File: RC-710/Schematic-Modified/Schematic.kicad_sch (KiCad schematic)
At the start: 66 parts, among them K1 Fujitsu_FTR-LYAA005x, Q1 NPN, Q2 NPN, SW1 ON/OFF, SW2 LEARN, U1 LM358, U2 4N25, Y1 Crystal

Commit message: Schematic: Improved layout
Signed-off-by: Patrick Pedersen <ctx.xda@gmail.com>
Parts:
- removed R25: R, symbol Device:R
- removed U2: 4N25, Package_DIP:DIP-6_W7.62mm, symbol Isolator:4N25
- added R13: R, symbol Device:R
- added R14: 5V: 380R / 3V3: 210R, symbol Device:R
- added U2: ~, symbol RC-710:Blob_IC
- added U3: 4N25, Package_DIP:DIP-6_W7.62mm, symbol Isolator:4N25
- Y1: value Crystal -> 455kHZ
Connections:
- net Blob IC PB LEARN: now also U2. (VCC)
- net Blob IC PB ON/OFF: now also U2. (VCC)
- net Blob IC REF CLK A: now also U2. (VCC)
- net Blob IC REF CLK B: now also U2. (VCC)
- net Blob IC SIGNAL: now also U2. (VCC)
- net GND: now also U2. (VCC), U3.4
- net Pi Pico W GND: now also U3.2
- net V1: no longer C11.1, C16.2, D10.2 (A), D13.1 (K), R16.1, R23.1, R7.1, U1.8 (V+)
- net Blob IC RST?: no longer names the net of TP2.1
- net Blob IC RST?: now also R13.1, U2. (VCC)
- net Blob IC UNKNOWN: no longer names the net of TP1.1
- net Blob IC UNKNOWN: now also U2. (VCC)
- net Blob IC VCC? renamed +3V0
- net +3V0: now also R13.2, U2. (VCC)
- net ~{Blob IC RELAY} renamed Blob IC RELAY
- net Blob IC RELAY: now also U2. (VCC), U3.6
- new net: R14.2, U3.1
- new net +5V: C11.1, C16.2, D10.2 (A), D13.1 (K), R16.1, R23.1, R7.1, U1.8 (V+)
- new net WiFi Board GPIO: R14.1
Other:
- note added: "Caution: May contain mistakes!"
- note added: "Handles device logic and RF signal processing"
- note added: "IC + Demod. Clock"
- note added: "IC Power"
- note added: "Mandolyn RC-710 Remote Power Socket"
- note added: "Misc"
- note added: "Power"
- note added: "Push Buttons"
- note added: "REMOVE"
- note added: "RF Circuit"
- note added: "Relay Switching"
- note added: "Schematic reverse engineered by: Patrick Pedersen"
- note added: "This device uses an unisolated power supply. This effectively means that all low voltages here are FLOATING AT MAINS VOLTAGE! Merely touching any GND terminal while the device is plugged in WILL SHOCK YOU with up to 325V!"
- note added: "Unknown Blob IC"
- note added: "WARNING: ELECTRICAL HAZARD"
- note added: "When testing the device it is highly recommended to connect a bench supply with 24VDC at betweem the recitfier output (C13) and GND. This eliminates the electrical hazard."
- note added: "WiFi Hack"
- note added: "~3V"
- note removed: "ADD"
- note removed: "CUT!"
- moved on the sheet: C1, C10, C14, C15, C17, C18, C19, C2, C3, C4, C5, C6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

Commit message: Modified Schematic: Minor change
Signed-off-by: Patrick Pedersen <ctx.xda@gmail.com>
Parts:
- R22: value R -> 10k
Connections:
- net Pi Pico W GND renamed WiFi Board GND
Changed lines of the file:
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@@
 		)
 	)
+	(polyline
+		(pts
+			(xy 278.13 233.68) (xy 278.13 219.71)
+		)
+		(stroke
+			(width 0)
+			(type dash)
+		)
+	)
 	(wire
 		(pts
@@
 		)
 	)
+	(text "REMOVE"
+		(exclude_from_sim no)
+		(at 273.304 221.742 0)
+		(effects
+			(font
+				(size 1.27 1.27)
+			)
+		)
+	)
 	(text "WiFi Hack"
 		(exclude_from_sim no)
@@
 			)
 		)
-		(property "Value" "R"
-			(at 278.892 223.52 90)
+		(property "Value" "10k"
+			(at 280.162 223.52 90)
 			(effects
 				(font
@@
 		(on_board yes)
 		(dnp no)
-		(fields_autoplaced yes)
 		(property "Reference" "#PWR031"
 			(at 346.71 227.33 0)
@@
 			)
 		)
-		(property "Value" "Pi Pico W GND"
-			(at 346.71 226.06 0)
+		(property "Value" "WiFi Board GND"
+			(at 339.09 226.06 0)
 			(effects
 				(font
 					(size 1.27 1.27)
 				)
+				(justify left)
 			)
 		)

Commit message: README: Added text
Signed-off-by: Patrick Pedersen <ctx.xda@gmail.com>
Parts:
- R14: value 5V: 380R / 3V3: 210R -> 5V: 380R / 3V3: 220R
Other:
- note added: "Bleeder"
- moved on the sheet: C13, R19
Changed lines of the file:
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@@
 	)
 	(junction
+		(at 55.88 43.18)
+		(diameter 0)
+		(color 0 0 0 0)
+	)
+	(junction
 		(at 138.43 58.42)
 		(diameter 0)
@@
 	)
 	(junction
-		(at 55.88 43.18)
-		(diameter 0)
-		(color 0 0 0 0)
-	)
-	(junction
 		(at 157.48 33.02)
 		(diameter 0)
@@
 	)
 	(junction
+		(at 71.12 43.18)
+		(diameter 0)
+		(color 0 0 0 0)
+	)
+	(junction
 		(at 59.69 168.91)
 		(diameter 0)
@@
 	)
 	(junction
-		(at 71.12 43.18)
-		(diameter 0)
-		(color 0 0 0 0)
-	)
-	(junction
 		(at 384.81 168.91)
 		(diameter 0)
@@
 	(wire
 		(pts
+			(xy 55.88 34.29) (xy 55.88 43.18)
+		)
+		(stroke
+			(width 0)
+			(type default)
+		)
+	)
+	(wire
+		(pts
 			(xy 180.34 168.91) (xy 187.96 168.91)
 		)
@@
 	(wire
 		(pts
+			(xy 67.31 34.29) (xy 71.12 34.29)
+		)
+		(stroke
+			(width 0)
+			(type default)
+		)
+	)
+	(wire
+		(pts
 			(xy 339.09 165.1) (xy 341.63 165.1)
 		)
@@
 	(wire
 		(pts
-			(xy 157.48 33.02) (xy 160.02 33.02)
+			(xy 71.12 43.18) (xy 85.09 43.18)
 		)
 		(stroke
@@
 	(wire
 		(pts
-			(xy 59.69 170.18) (xy 59.69 168.91)
+			(xy 157.48 33.02) (xy 160.02 33.02)
 		)
 		(stroke
@@
 	(wire
 		(pts
-			(xy 217.17 165.1) (xy 217.17 168.91)
+			(xy 59.69 170.18) (xy 59.69 168.91)
 		)
 		(stroke
@@
 		)
 	)
-	(polyline
+	(wire
 		(pts
-			(xy 199.39 68.58) (xy 407.67 68.58)
+			(xy 217.17 165.1) (xy 217.17 168.91)
 		)
 		(stroke
@@
 		)
 	)
-	(wire
+	(polyline
 		(pts
-			(xy 40.64 133.35) (xy 53.34 133.35)
+			(xy 199.39 68.58) (xy 407.67 68.58)
 		)
 		(stroke
@@
 	(wire
 		(pts
-			(xy 171.45 196.85) (xy 171.45 186.69)
+			(xy 40.64 133.35) (xy 53.34 133.35)
 		)
 		(stroke
@@
 	(wire
 		(pts
-			(xy 55.88 43.18) (xy 55.88 49.53)
+			(xy 171.45 196.85) (xy 171.45 186.69)
 		)
 		(stroke
@@
 	(wire
 		(pts
-			(xy 71.12 43.18) (xy 71.12 49.53)
-		)
-		(stroke
-			(width 0)
-			(type default)
-		)
-	)
-	(wire
-		(pts
 			(xy 195.58 168.91) (xy 204.47 168.91)
 		)
@@
 	(wire
 		(pts
-			(xy 67.31 43.18) (xy 71.12 43.18)
-		)
-		(stroke
-			(width 0)
-			(type default)
-		)
-	)
-	(wire
-		(pts
 			(xy 367.03 168.91) (xy 384.81 168.91)
 		)
@@
 	(wire
 		(pts
-			(xy 71.12 43.18) (xy 85.09 43.18)
-		)
-		(stroke
-			(width 0)
-			(type default)
-		)
-	)
-	(wire
-		(pts
 			(xy 242.57 245.11) (xy 242.57 247.65)
 		)
@@
 	(wire
 		(pts
-			(xy 55.88 49.53) (xy 59.69 49.53)
-		)
-		(stroke
-			(width 0)
-			(type default)
-		)
-	)
-	(wire
-		(pts
 			(xy 170.18 231.14) (xy 180.34 231.14)
 		)
@@
 	(wire
 		(pts
-			(xy 67.31 49.53) (xy 71.12 49.53)
+			(xy 67.31 43.18) (xy 71.12 43.18)
 		)
 		(stroke
@@
 	(wire
 		(pts
+			(xy 55.88 34.29) (xy 59.69 34.29)
+		)
+		(stroke
+			(width 0)
+			(type default)
+		)
+	)
+	(wire
+		(pts
 			(xy 99.06 58.42) (xy 105.41 58.42)
 		)
@@
 	(wire
 		(pts
-			(xy 55.88 43.18) (xy 59.69 43.18)
-		)
-		(stroke
-			(width 0)
-			(type default)
-		)
-	)
-	(wire
-		(pts
 			(xy 198.12 245.11) (xy 208.28 245.11)
 		)
@@
 	(wire
 		(pts
+			(xy 71.12 34.29) (xy 71.12 43.18)
+		)
+		(stroke
+			(width 0)
+			(type default)
+		)
+	)
+	(wire
+		(pts
 			(xy 242.57 231.14) (xy 242.57 237.49)
 		)
@@
 		)
 	)
+	(wire
+		(pts
+			(xy 55.88 43.18) (xy 59.69 43.18)
+		)
+		(stroke
+			(width 0)
+			(type default)
+		)
+	)
 	(rectangle
 		(start 157.48 63.5)
@@
 		)
 	)
+	(text "Bleeder"
+		(exclude_from_sim no)
+		(at 63.5 36.83 0)
+		(effects
+			(font
+				(size 1.27 1.27)
+			)
+		)
+	)
 	(text "WARNING: ELECTRICAL HAZARD"
 		(exclude_from_sim no)
@@
 			)
 		)
-		(property "Value" "5V: 380R / 3V3: 210R"
+		(property "Value" "5V: 380R / 3V3: 220R"
 			(at 337.82 208.28 90)
 			(effects
@@
 	(symbol
 		(lib_id "Device:C")
-		(at 63.5 49.53 90)
+		(at 63.5 43.18 90)
 		(unit 1)
 		(exclude_from_sim no)
@@
 		(dnp no)
 		(property "Reference" "C13"
-			(at 63.5 54.61 90)
+			(at 63.5 48.26 90)
 			(effects
 				(font
@@
 		)
 		(property "Value" "0.22uF"
-			(at 63.5 57.15 90)
+			(at 63.5 50.8 90)
 			(effects
 				(font
@@
 		)
 		(property "Footprint" ""
-			(at 67.31 48.5648 0)
+			(at 67.31 42.2148 0)
 			(effects
 				(font
@@
 		)
 		(property "Datasheet" "~"
-			(at 63.5 49.53 0)
+			(at 63.5 43.18 0)
 			(effects
 				(font
@@
 		)
 		(property "Description" "Unpolarized capacitor"
-			(at 63.5 49.53 0)
+			(at 63.5 43.18 0)
 			(effects
 				(font
@@
 	(symbol
 		(lib_id "Device:R")
-		(at 63.5 43.18 90)
+		(at 63.5 34.29 90)
 		(unit 1)
 		(exclude_from_sim no)
@@
 		(fields_autoplaced yes)
 		(property "Reference" "R19"
-			(at 63.5 36.83 90)
+			(at 63.5 27.94 90)
 			(effects
 				(font
@@
 		)
 		(property "Value" "1M"
-			(at 63.5 39.37 90)
+			(at 63.5 30.48 90)
 			(effects
 				(font
@@
 		)
 		(property "Footprint" ""
-			(at 63.5 44.958 90)
+			(at 63.5 36.068 90)
 			(effects
 				(font
@@
 		)
 		(property "Datasheet" "~"
-			(at 63.5 43.18 0)
+			(at 63.5 34.29 0)
 			(effects
 				(font
@@
 		)
 		(property "Description" "Resistor"
-			(at 63.5 43.18 0)
+			(at 63.5 34.29 0)
 			(effects
 				(font

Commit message: README: Updated + Schematic: Minor correction
Signed-off-by: Patrick Pedersen <ctx.xda@gmail.com>
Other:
- note added: "IC Clock"
- note removed: "IC + Demod. Clock"
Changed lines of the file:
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@@
 		)
 	)
-	(text "IC + Demod. Clock"
+	(text "IC Clock"
 		(exclude_from_sim no)
 		(at 104.14 97.79 0)

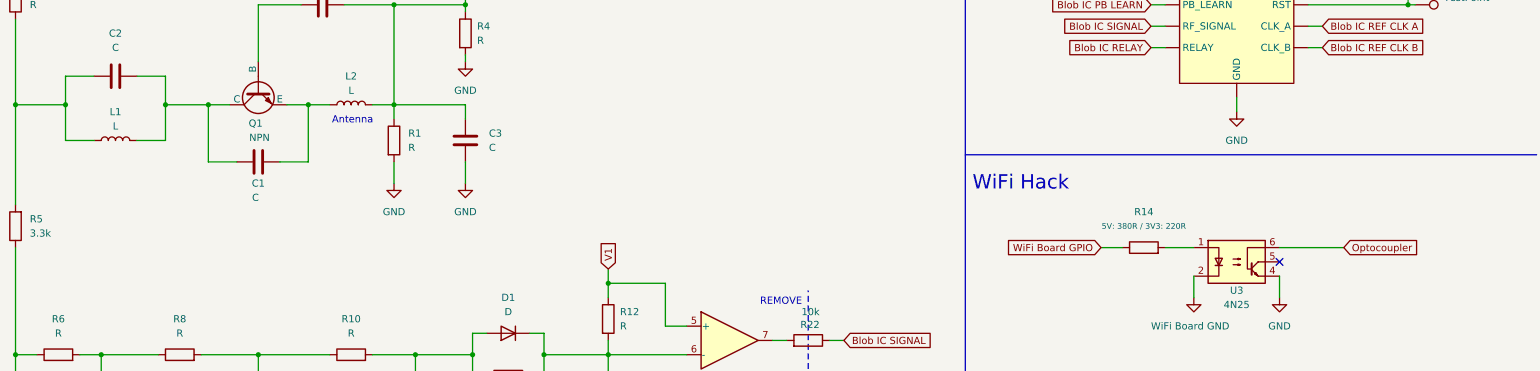
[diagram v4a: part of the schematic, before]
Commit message: Fix wrong optocoupler wiring
Signed-off-by: Patrick Pedersen <ctx.xda@gmail.com>
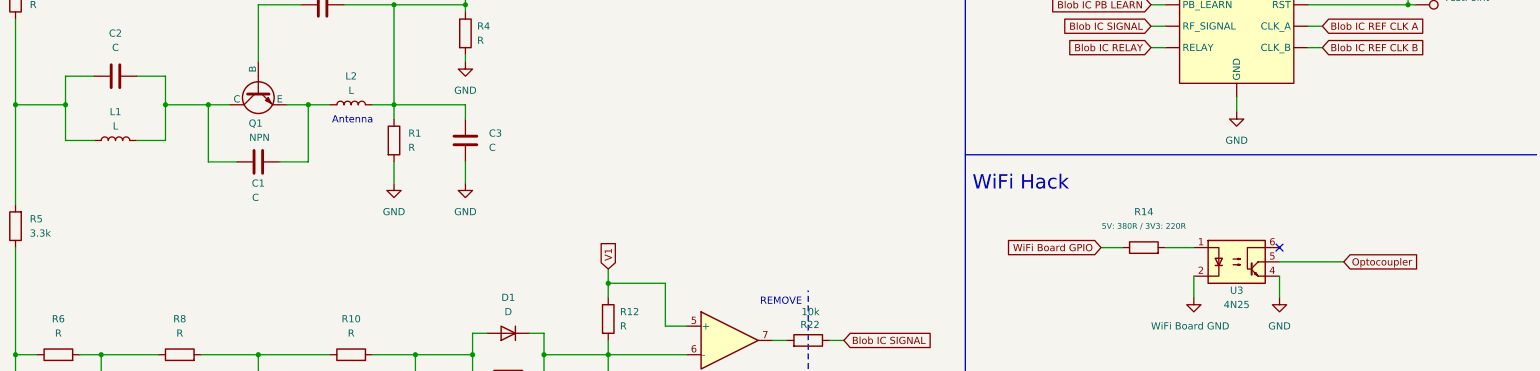
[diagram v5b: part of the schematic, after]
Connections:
- net Blob IC RELAY: now also U3.5; no longer U3.6
